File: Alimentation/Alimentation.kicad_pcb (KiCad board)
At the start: 2 copper layers, 56 x 86 mm, 8 parts, among them J1 RPI, J2 STEPPER, J3 LORA, J4 BATTERY RPI EXPE, J5 BATTERY LORA, J6 RPI_VOUT, J7 STEPPER_VOUT, J8 LORA_VOUT

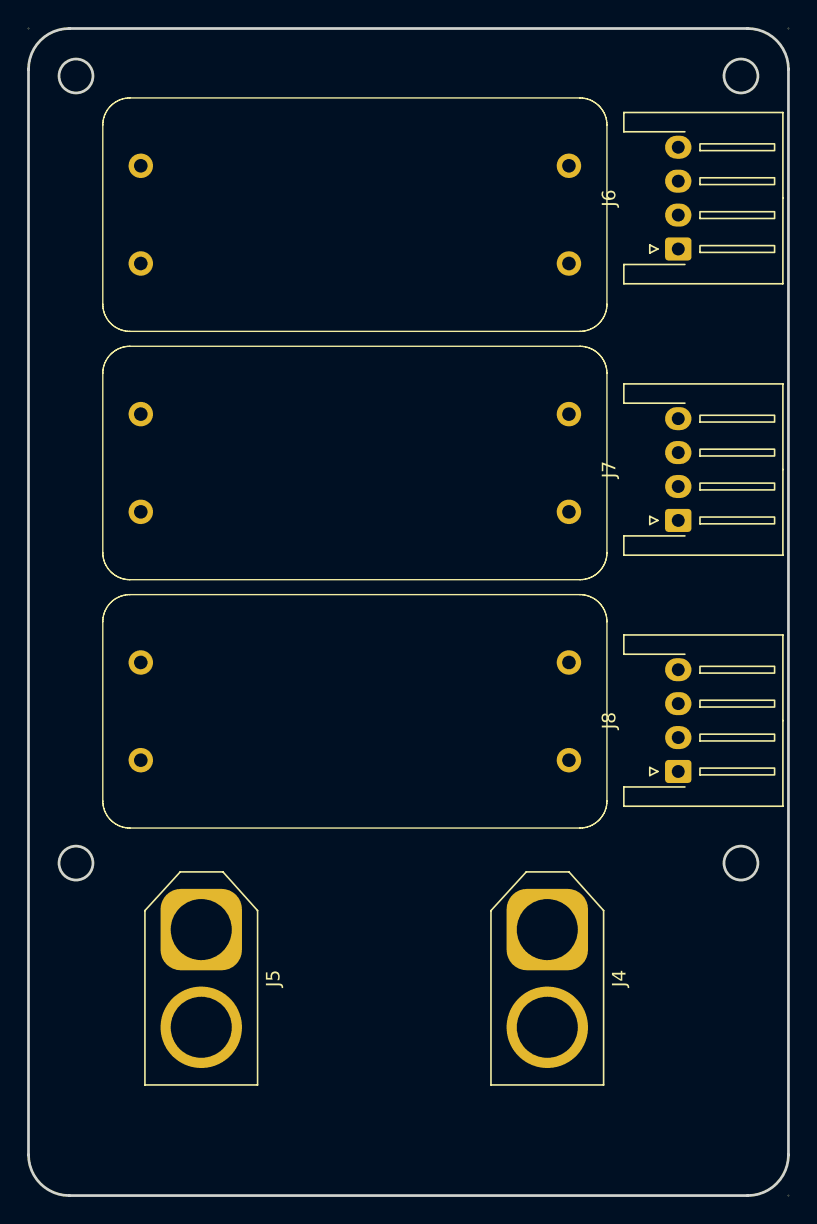
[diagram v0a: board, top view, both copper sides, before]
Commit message: Routed Power Board
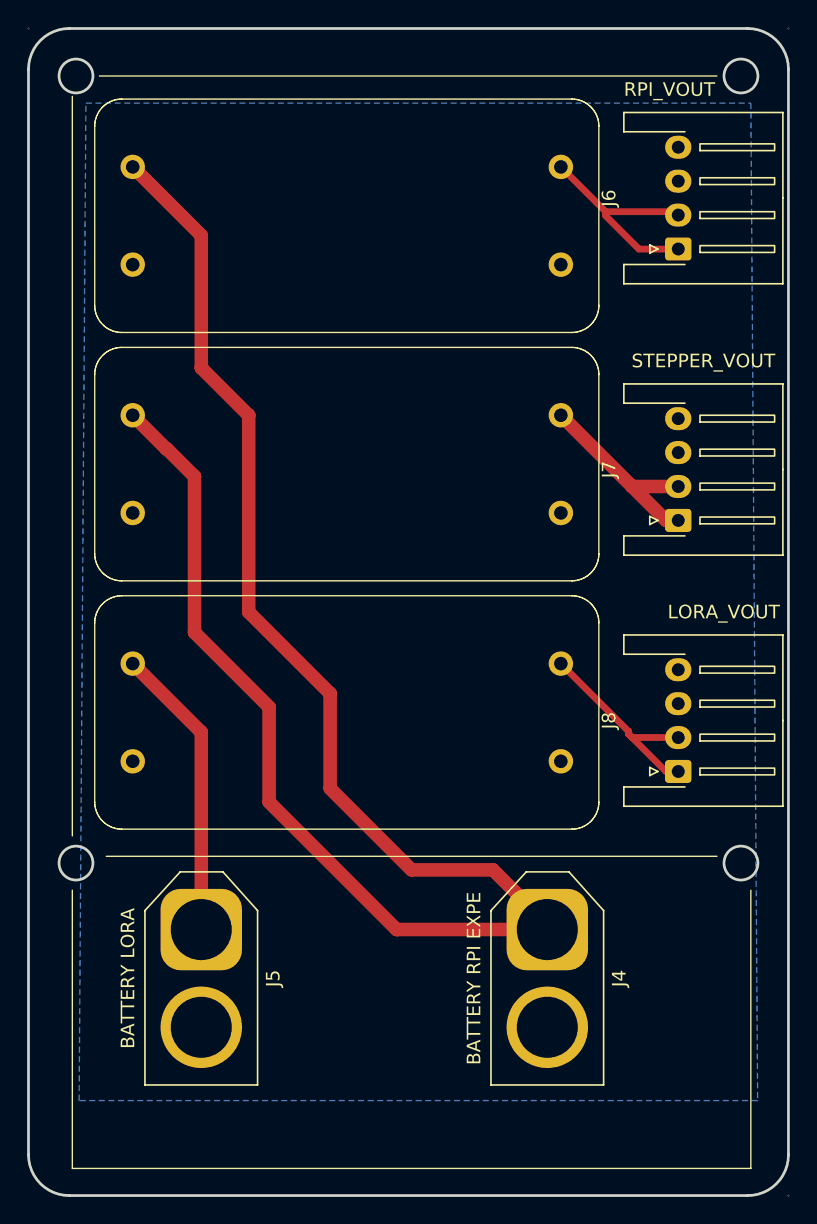
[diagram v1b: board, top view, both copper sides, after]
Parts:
- turned J1 to 0 degrees
- turned J2 to 0 degrees
- turned J3 to 0 degrees
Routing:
- net +VIN_RPI: track 0.00 -> 129.5 mm
- net +VIN_LORA: track 0.00 -> 21.7 mm
- net +5V_RPI: track 0.00 -> 18.2 mm
- net +3V3_LORA: track 0.00 -> 15.8 mm
- net +VOUT_STEPPER: track 0.00 -> 15.3 mm
- added copper zone on B.Cu, net GND

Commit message: Fully Routed Sensor board
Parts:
- added H1: MountingHole_Pad, MountingHole:MountingHole_3.2mm_M3_DIN965_Pad, F.Cu at (184.2, 48.5)
- added H2: MountingHole_Pad, MountingHole:MountingHole_3.2mm_M3_DIN965_Pad, F.Cu at (120.2, 48.5)
- added H3: MountingHole_Pad, MountingHole:MountingHole_3.2mm_M3_DIN965_Pad, F.Cu at (184.2, 125.5)
- added H4: MountingHole_Pad, MountingHole:MountingHole_3.2mm_M3_DIN965_Pad, F.Cu at (120.2, 125.5)
- added J10: BATTERY PARACHUTE, PHOENIX_CON:AMASS_XT60-M_1x02_P7.20mm_Vertical, B.Cu at (145.7, 112.1)
- added J11: STEPPER_VOUT, Connector_JST:JST_XH_S4B-XH-A-1_1x04_P2.50mm_Horizontal, B.Cu at (172.0, 115.6)
- added J9: PARACHUTE, PHOENIX:BUCK_STEPDOWN_LM2592, F.Cu at (149.1, 117.2)
- J1: footprint PHOENIX:MT3608 -> PHOENIX:BUCK_STEPDOWN_LM2592; moved to B.Cu
- J2, J3: footprint PHOENIX:MT3608 -> PHOENIX:BUCK_STEPDOWN_LM2592
- J4, J5, J6, J7, J8: moved to B.Cu
- moved J8 47.0 mm to (164.8, 52.4), turned to 0 degrees
- moved J6 40.5 mm to (132.4, 52.5), turned to 0 degrees
- moved J7 36.3 mm to (148.8, 52.5), turned to 0 degrees
- moved J3 30.9 mm to (176.3, 81.8), turned to 90 degrees
- moved J1 24.2 mm to (151.5, 81.7), turned to 90 degrees
- moved J2 20.9 mm to (127.9, 81.7), turned to 90 degrees
- moved J4 4.61 mm to (158.4, 112.5)
- moved J5 3.94 mm to (133.5, 112.2)
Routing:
- net +VIN_RPI: track 129.5 -> 0.00 mm
- net +VIN_LORA: track 21.7 -> 0.00 mm
- net +5V_RPI: track 18.2 -> 0.00 mm
- net +3V3_LORA: track 15.8 -> 0.00 mm
- net +VOUT_STEPPER: track 15.3 -> 0.00 mm
- removed copper zone on B.Cu, net GND
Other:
- board size 56 x 86 mm -> 21 x 43 mm

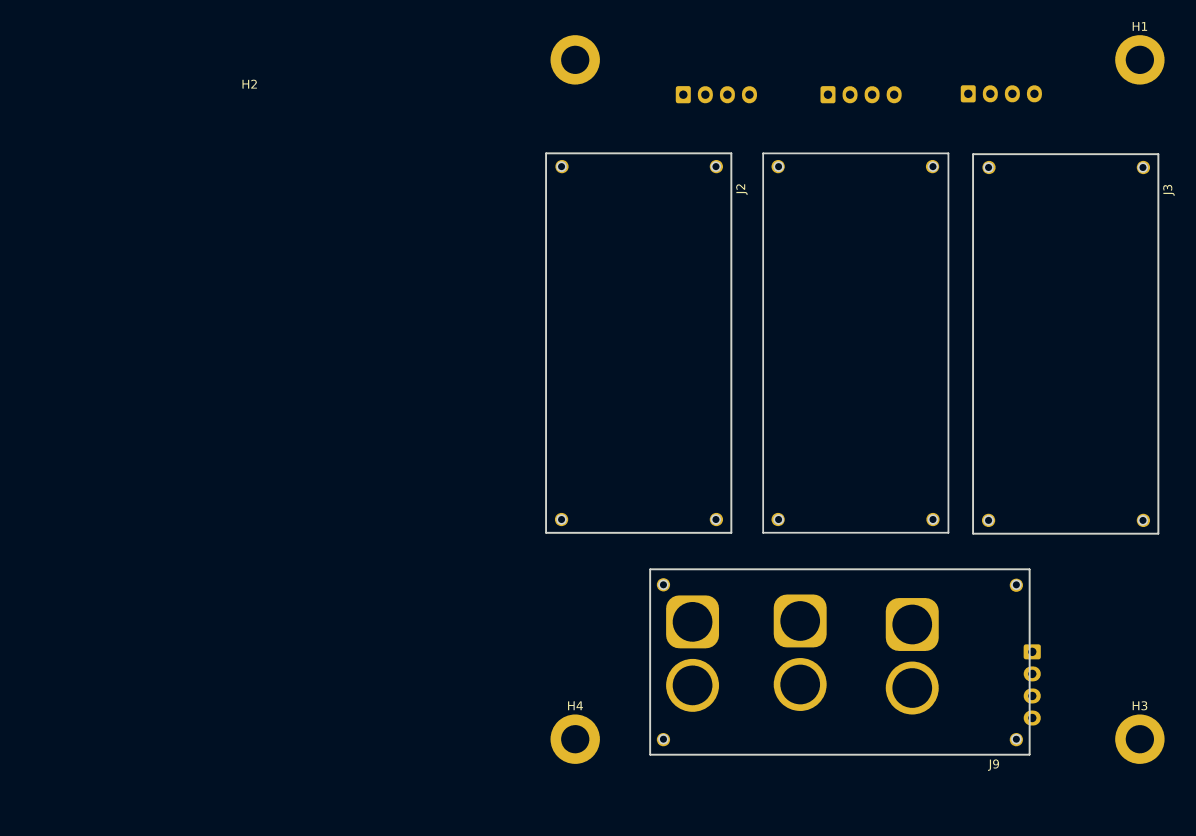
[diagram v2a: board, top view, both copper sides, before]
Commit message: flipped connections for the GPS connector to 3_3,RX <-> GND,TX
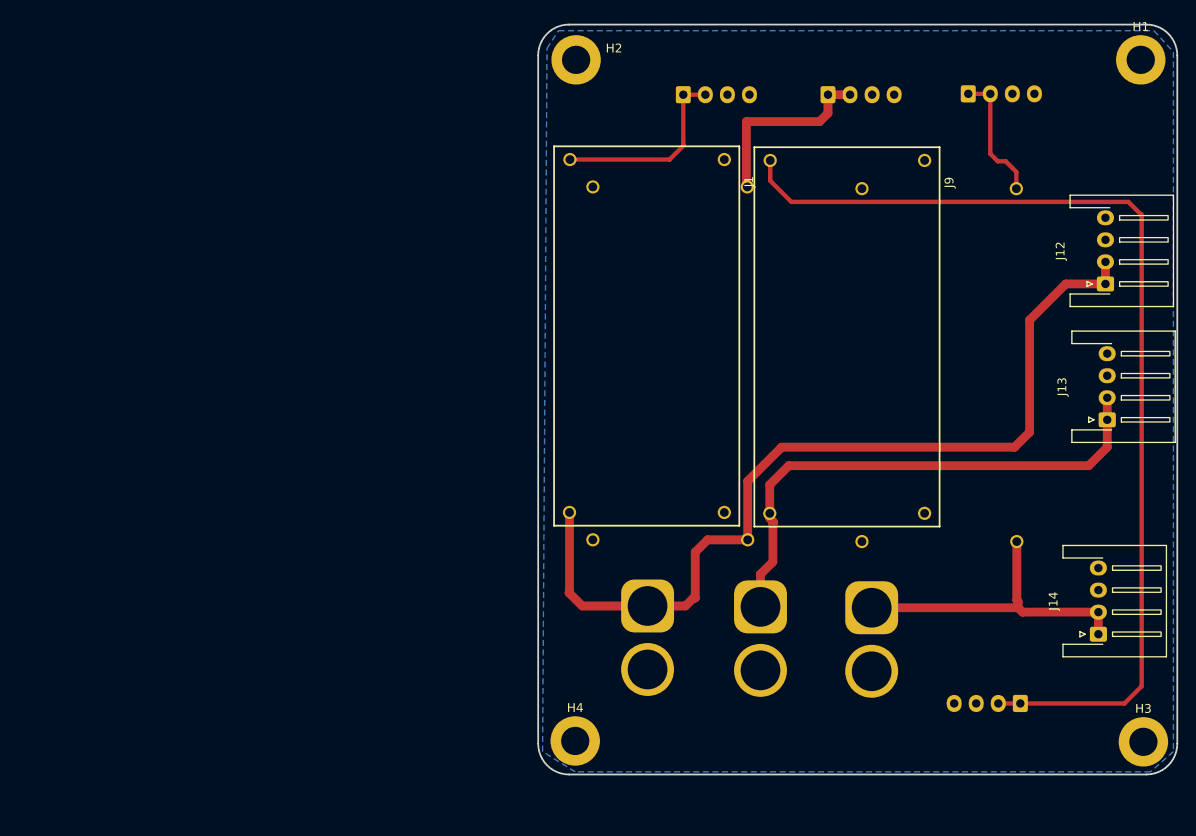
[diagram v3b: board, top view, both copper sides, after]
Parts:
- added J12: SWITCH_RPI, Connector_JST:JST_XH_S4B-XH-A-1_1x04_P2.50mm_Horizontal, F.Cu at (180.3, 73.9)
- added J13: SWITCH_PARA, Connector_JST:JST_XH_S4B-XH-A-1_1x04_P2.50mm_Horizontal, F.Cu at (180.5, 89.3)
- added J14: SWITCH_LORA, Connector_JST:JST_XH_S4B-XH-A-1_1x04_P2.50mm_Horizontal, F.Cu at (179.5, 113.6)
- J1: moved to F.Cu
- J2, J3: moved to B.Cu
- moved J9 36.3 mm to (151.5, 81.0), turned to 90 degrees
- moved J4 30.1 mm to (128.4, 110.4)
- moved J1 22.7 mm to (128.8, 80.9)
- moved J5 20.4 mm to (153.8, 110.6)
- moved J3 15.5 mm to (161.0, 84.2)
- moved J11 6.00 mm to (170.7, 121.5), turned to 180 degrees
- moved J10 4.78 mm to (141.2, 110.5)
- moved J2 3.47 mm to (130.5, 84.0)
- moved H3 0.50 mm to (184.6, 125.8)
- moved H4 0.20 mm to (120.2, 125.7)
- moved H1 0.10 mm to (184.3, 48.5)
- moved H2 0.10 mm to (120.3, 48.5)
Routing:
- net +5V_PARA: track 0.00 -> 116.4 mm
- net +VIN_RPI: track 0.00 -> 102.5 mm
- net +VIN_PARA: track 0.00 -> 60.3 mm
- net +VIN_LORA: track 0.00 -> 36.0 mm
- net +5V_RPI: track 0.00 -> 21.8 mm
- net +VOUT_STEPPER: track 0.00 -> 21.7 mm
- net +3V3_LORA: track 0.00 -> 15.0 mm
- added copper zone on B.Cu, net GND
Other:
- board size 21 x 43 mm -> 72.4 x 85 mm

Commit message: alimentation: full revision
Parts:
- removed H3, H4: MountingHole_Pad, MountingHole:MountingHole_3.2mm_M3_DIN965_Pad
- added H5: MountingHole_3.2mm_M3, MountingHole:MountingHole_3.2mm_M3, F.Cu at (61.0, 130.5)
- added H6: MountingHole_3.2mm_M3, MountingHole:MountingHole_3.2mm_M3, F.Cu at (120.0, 130.5)
- H1, H2: value MountingHole_Pad -> MountingHole_3.2mm_M3; footprint MountingHole:MountingHole_3.2mm_M3_DIN965_Pad -> MountingHole:MountingHole_3.2mm_M3
- J1: footprint PHOENIX:BUCK_STEPDOWN_LM2592 -> nasa:LM2596
- J10, J4, J5: footprint PHOENIX_CON:AMASS_XT60-M_1x02_P7.20mm_Vertical -> Connector_AMASS:AMASS_XT60PW-M_1x02_P7.20mm_Horizontal; moved to F.Cu
- J11: value STEPPER_VOUT -> PARACHUTE_VOUT; footprint Connector_JST:JST_XH_S4B-XH-A-1_1x04_P2.50mm_Horizontal -> Connector_JST:JST_XH_S4B-XH-A_1x04_P2.50mm_Horizontal; moved to F.Cu
- J12, J13, J14: footprint Connector_JST:JST_XH_S4B-XH-A-1_1x04_P2.50mm_Horizontal -> Connector_JST:JST_XH_B4B-XH-A_1x04_P2.50mm_Vertical
- J2, J3: footprint PHOENIX:BUCK_STEPDOWN_LM2592 -> nasa:LM2596; moved to F.Cu
- J6, J7, J8: footprint Connector_JST:JST_XH_S4B-XH-A-1_1x04_P2.50mm_Horizontal -> Connector_JST:JST_XH_S4B-XH-A_1x04_P2.50mm_Horizontal; moved to F.Cu
- J9: footprint PHOENIX:BUCK_STEPDOWN_LM2592 -> nasa:LM2596; moved to B.Cu
- moved J12 129.2 mm to (61.0, 123.5)
- moved H1 123.3 mm to (61.0, 50.0)
- moved J3 84.4 mm to (78.7, 102.9), turned to 0 degrees
- moved J13 77.1 mm to (105.5, 107.0)
- moved J8 75.3 mm to (113.1, 107.1), turned to 90 degrees
- moved J11 64.3 mm to (113.0, 93.0), turned to 90 degrees
- moved J9 60.6 mm to (90.9, 81.5)
- moved J14 59.5 mm to (120.0, 115.5), turned to -90 degrees
- moved J2 51.9 mm to (78.7, 80.6), turned to 0 degrees
- moved J4 51.6 mm to (77.1, 116.3), turned to 180 degrees
- moved J1 48.6 mm to (85.7, 58.4), turned to 0 degrees
- moved J10 47.5 mm to (94.1, 116.3), turned to 180 degrees
- moved J7 44.4 mm to (113.1, 78.8), turned to 90 degrees
- moved J5 43.1 mm to (111.1, 116.3), turned to 180 degrees
- moved J6 23.0 mm to (113.1, 64.8), turned to 90 degrees
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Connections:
- J1 pad 1: +VIN_RPI -> +VCC_RPI
- J10 pad 2: GND -> GND1
- J11 pad 3: GND -> GND1
- J11 pad 4: GND -> GND1
- J12 pad 3: GND -> +VCC_RPI
- J12 pad 4: GND -> +VCC_RPI
- J13 pad 3: GND -> +VCC_PARA
- J13 pad 4: GND -> +VCC_PARA
- J14 pad 3: GND -> +VCC_LORA
- J14 pad 4: GND -> +VCC_LORA
- J2 pad 1: +VIN_RPI -> +VCC_RPI
- J3 pad 1: +VIN_LORA -> +VCC_LORA
- J9 pad 1: +VIN_PARA -> +VCC_PARA
- J9 pad 3: GND -> GND1
- J9 pad 4: GND -> GND1
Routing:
- net GND1: track 0.00 -> 96.5 mm
- net +VIN_RPI: track 102.5 -> 22.4 mm
- net +5V_PARA: track 116.4 -> 40.4 mm
- net +VCC_RPI: track 0.00 -> 75.5 mm
- net +VCC_LORA: track 0.00 -> 73.8 mm
- net +VIN_PARA: track 60.3 -> 20.5 mm
- net +VIN_LORA: track 36.0 -> 11.8 mm
- net +VCC_PARA: track 0.00 -> 8.19 mm
- net +3V3_LORA: track 15.0 -> 21.4 mm
- net +VOUT_STEPPER: track 21.7 -> 17.7 mm
- net +5V_RPI: track 21.8 -> 20.6 mm
- added copper zone on F.Cu, net GND
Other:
- board size 72.4 x 85 mm -> 65 x 86.5 mm
- board text added: "BATTERY"
- board text added: "LORA"
- board text added: "PARACHUTE"
- board text added: "RASPI"
- board text added: "STEPPER"
- board text added: "SW LORA"
- board text added: "SW PARACHUTE"
- board text added: "SW RASPI"
